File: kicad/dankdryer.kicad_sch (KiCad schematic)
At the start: 20 parts, among them J13 barreljack, J9 UART, SW2 boot, U4 TPS62132RGTR, U6 ESP32-C6-MINI-1U

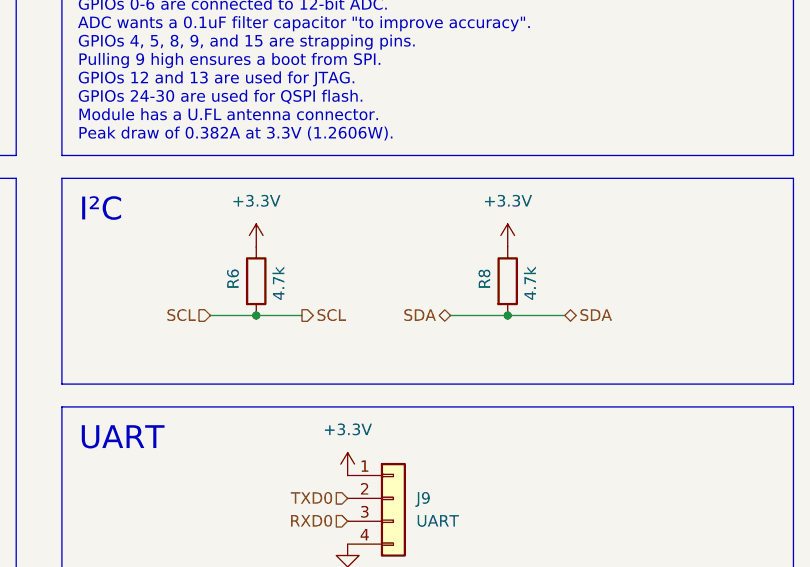
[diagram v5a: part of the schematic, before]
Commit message: move to 2.2k resistors for I2C
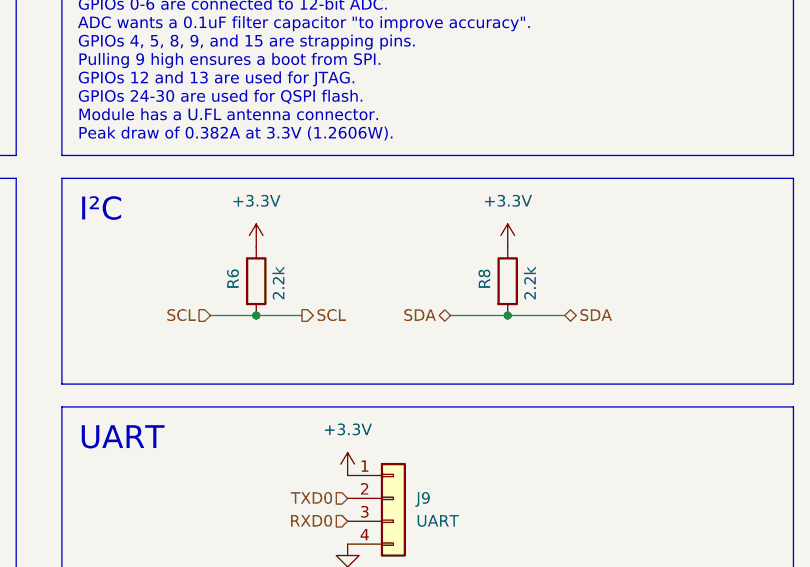
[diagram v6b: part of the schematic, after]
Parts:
- R6, R8: value 4.7k -> 2.2k
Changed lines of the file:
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@@
 	(title_block
 		(title "dankdryer")
-		(date "2025-03-18")
-		(rev "2.1.0")
+		(date "2025-03-26")
+		(rev "2.1.1")
 		(company "dirty south supercomputing")
 		(comment 1 "nick black")
@@
 			)
 		)
-		(property "Value" "4.7k"
+		(property "Value" "2.2k"
 			(at 222.25 123.444 90)
 			(effects
@@
 			)
 		)
-		(property "Value" "4.7k"
+		(property "Value" "2.2k"
 			(at 194.31 123.444 90)
 			(effects

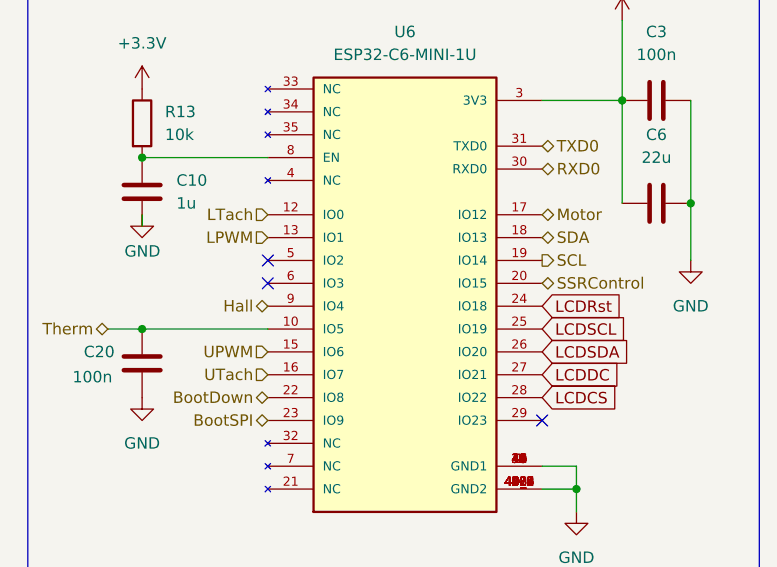
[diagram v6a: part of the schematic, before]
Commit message: elaborate layout changes to eliminate a voltage divider
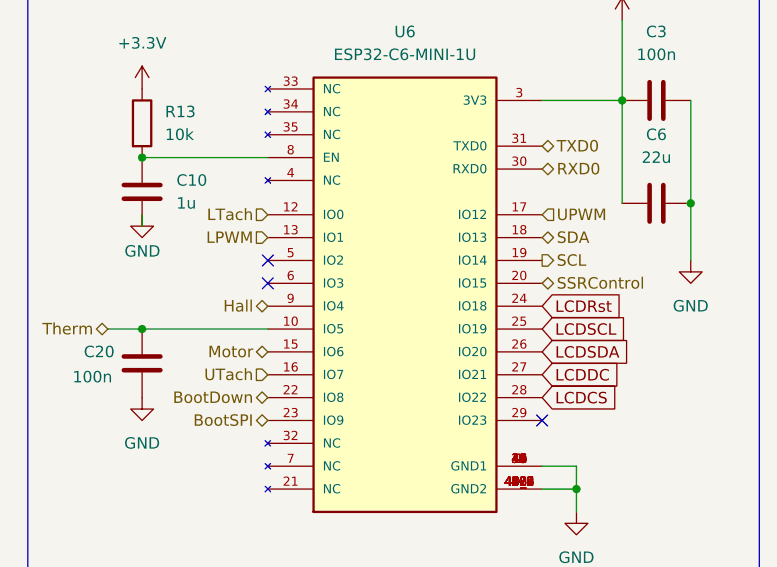
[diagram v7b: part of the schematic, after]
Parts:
- R6, R8: footprint Resistor_SMD:R_0805_2012Metric_Pad1.20x1.40mm_HandSolder -> Resistor_SMD:R_1206_3216Metric_Pad1.30x1.75mm_HandSolder
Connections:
- net Motor: now also U6.15 (IO6); no longer U6.17 (IO12)
- net UPWM: now also U6.17 (IO12); no longer U6.15 (IO6)
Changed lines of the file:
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@@
 	(wire
 		(pts
+			(xy 182.88 60.96) (xy 196.85 60.96)
+		)
+		(stroke
+			(width 0)
+			(type default)
+		)
+	)
+	(wire
+		(pts
 			(xy 129.54 36.83) (xy 129.54 31.75)
 		)
@@
 	(wire
 		(pts
-			(xy 182.88 60.96) (xy 196.85 60.96)
-		)
-		(stroke
-			(width 0)
-			(type default)
-		)
-	)
-	(wire
-		(pts
 			(xy 140.97 31.75) (xy 146.05 31.75)
 		)
@@
 		)
 	)
-	(hierarchical_label "LPWM"
+	(hierarchical_label "LTach"
 		(shape input)
-		(at 196.85 50.8 180)
+		(at 196.85 48.26 180)
 		(effects
 			(font
@@
 		)
 	)
-	(hierarchical_label "Motor"
+	(hierarchical_label "Hall"
 		(shape bidirectional)
-		(at 227.33 48.26 0)
+		(at 64.77 147.32 0)
 		(effects
 			(font
@@
 		)
 	)
-	(hierarchical_label "Hall"
+	(hierarchical_label "Motor"
 		(shape bidirectional)
-		(at 64.77 147.32 0)
+		(at 196.85 63.5 180)
 		(effects
 			(font
 				(size 1.27 1.27)
 			)
-			(justify left)
+			(justify right)
 		)
 	)
@@
 		)
 	)
+	(hierarchical_label "UTach"
+		(shape input)
+		(at 196.85 66.04 180)
+		(effects
+			(font
+				(size 1.27 1.27)
+			)
+			(justify right)
+		)
+	)
 	(hierarchical_label "BootDown"
 		(shape bidirectional)
@@
 		)
 	)
+	(hierarchical_label "UPWM"
+		(shape input)
+		(at 227.33 48.26 0)
+		(effects
+			(font
+				(size 1.27 1.27)
+			)
+			(justify left)
+		)
+	)
 	(hierarchical_label "LTach"
 		(shape input)
@@
 		)
 	)
-	(hierarchical_label "UPWM"
+	(hierarchical_label "LPWM"
 		(shape input)
-		(at 196.85 63.5 180)
+		(at 196.85 50.8 180)
 		(effects
 			(font
@@
 		)
 	)
-	(hierarchical_label "LTach"
-		(shape input)
-		(at 196.85 48.26 180)
-		(effects
-			(font
-				(size 1.27 1.27)
-			)
-			(justify right)
-		)
-	)
-	(hierarchical_label "UTach"
-		(shape input)
-		(at 196.85 66.04 180)
-		(effects
-			(font
-				(size 1.27 1.27)
-			)
-			(justify right)
-		)
-	)
 	(hierarchical_label "Therm"
 		(shape input)
@@
 			)
 		)
-		(property "Footprint" "Resistor_SMD:R_0805_2012Metric_Pad1.20x1.40mm_HandSolder"
+		(property "Footprint" "Resistor_SMD:R_1206_3216Metric_Pad1.30x1.75mm_HandSolder"
 			(at 217.932 123.19 90)
 			(effects
@@
 			)
 		)
-		(property "Footprint" "Resistor_SMD:R_0805_2012Metric_Pad1.20x1.40mm_HandSolder"
+		(property "Footprint" "Resistor_SMD:R_1206_3216Metric_Pad1.30x1.75mm_HandSolder"
 			(at 189.992 123.19 90)
 			(effects

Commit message: v2.1.5
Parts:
- C3: footprint Capacitor_SMD:C_0805_2012Metric_Pad1.18x1.45mm_HandSolder -> Capacitor_SMD:C_1206_3216Metric_Pad1.33x1.80mm_HandSolder
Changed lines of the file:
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@@
 	(title_block
 		(title "dankdryer")
-		(date "2025-03-26")
-		(rev "2.1.1")
+		(date "2025-03-27")
+		(rev "2.1.5")
 		(company "dirty south supercomputing")
 		(comment 1 "nick black")
@@
 			)
 		)
-		(property "Footprint" "Capacitor_SMD:C_0805_2012Metric_Pad1.18x1.45mm_HandSolder"
+		(property "Footprint" "Capacitor_SMD:C_1206_3216Metric_Pad1.33x1.80mm_HandSolder"
 			(at 243.84 34.5948 0)
 			(effects
